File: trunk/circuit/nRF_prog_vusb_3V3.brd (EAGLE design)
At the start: 50 x 50 mm, 26 parts, among them Q2 12MHz

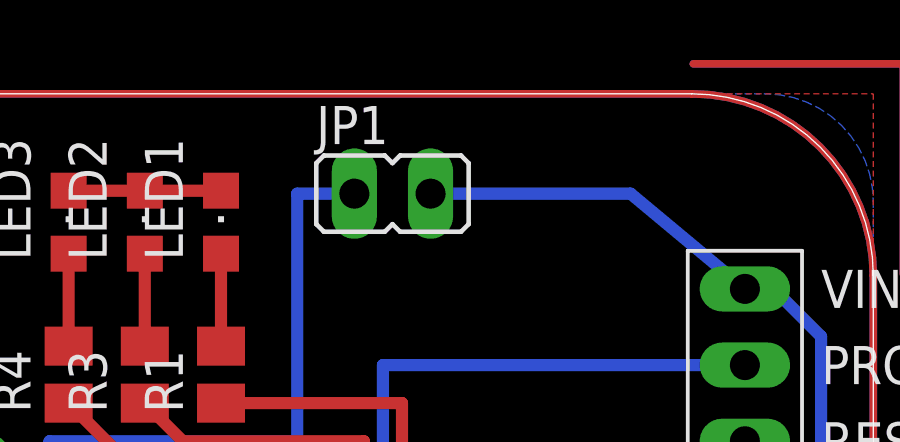
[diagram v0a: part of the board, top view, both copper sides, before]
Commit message: 
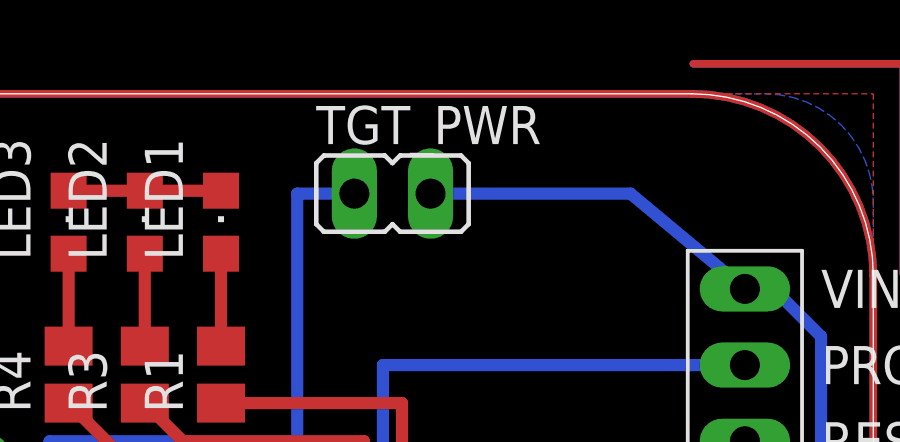
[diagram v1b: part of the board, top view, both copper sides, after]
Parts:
- renumbered JP1 to TGT_PWR
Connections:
- new net NRF_RESET: U$2.RESET
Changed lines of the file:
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@@
 <element name="LED1" library="led" package="CHIPLED_0805" value="" x="28.2575" y="45.72"/>
 <element name="R1" library="rcl" package="M0805" value="" x="28.2575" y="40.64" rot="R90"/>
-<element name="JP1" library="KileParts" package="JP1" value="TGT_PWR" x="33.9725" y="46.6725" rot="R270"/>
+<element name="TGT_PWR" library="KileParts" package="JP1" value="TGT_PWR" x="33.9725" y="46.6725" rot="R270"/>
 <element name="C2" library="rcl" package="C0805K" value="470nF" x="14.605" y="20.6375"/>
 <element name="R2" library="rcl" package="M0805" value="10K" x="18.7325" y="13.97" rot="R270"/>
@@
 <signal name="VIN">
 <contactref element="NRF_GEN" pad="VUSB"/>
-<contactref element="JP1" pad="2"/>
+<contactref element="TGT_PWR" pad="2"/>
 <contactref element="U$2" pad="VIN"/>
 <contactref element="C5" pad="+"/>
@@
 <contactref element="LM3940" pad="1"/>
 <contactref element="C2" pad="1"/>
-<contactref element="JP1" pad="1"/>
+<contactref element="TGT_PWR" pad="1"/>
 <wire x1="9.545" y1="40.2463" x2="9.545" y2="36.83" width="0.4064" layer="16"/>
 <wire x1="30.7975" y1="38.4175" x2="30.7975" y2="46.6725" width="0.4064" layer="16"/>
@@
 <wire x1="51" y1="-1" x2="44" y2="-1" width="0.254" layer="16"/>
 </signal>
+<signal name="NRF_RESET">
+<contactref element="U$2" pad="RESET"/>
+</signal>
 </signals>

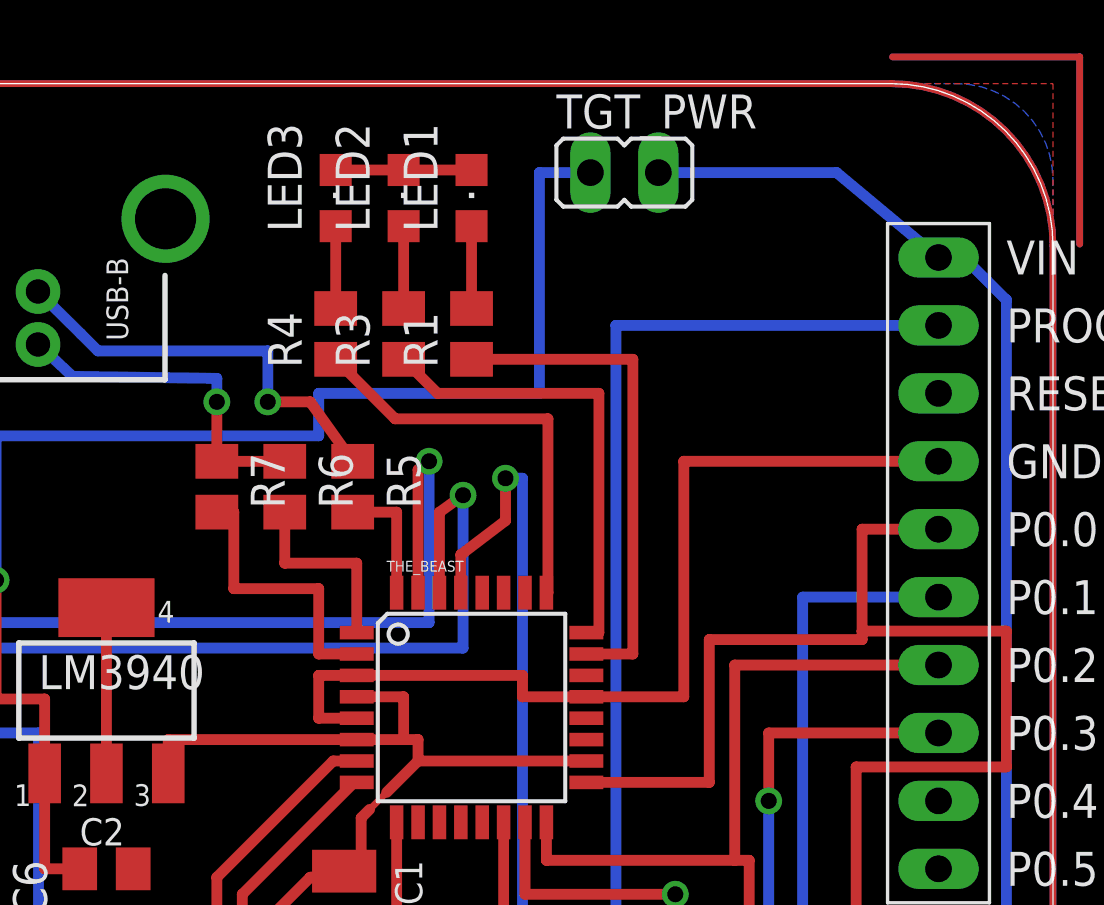
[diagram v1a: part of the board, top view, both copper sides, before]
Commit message: New version works uses reset which hopefully fixes the problems with programming nRF24LU1+ It looks like it is necessary to reset the target before and/or after programming.
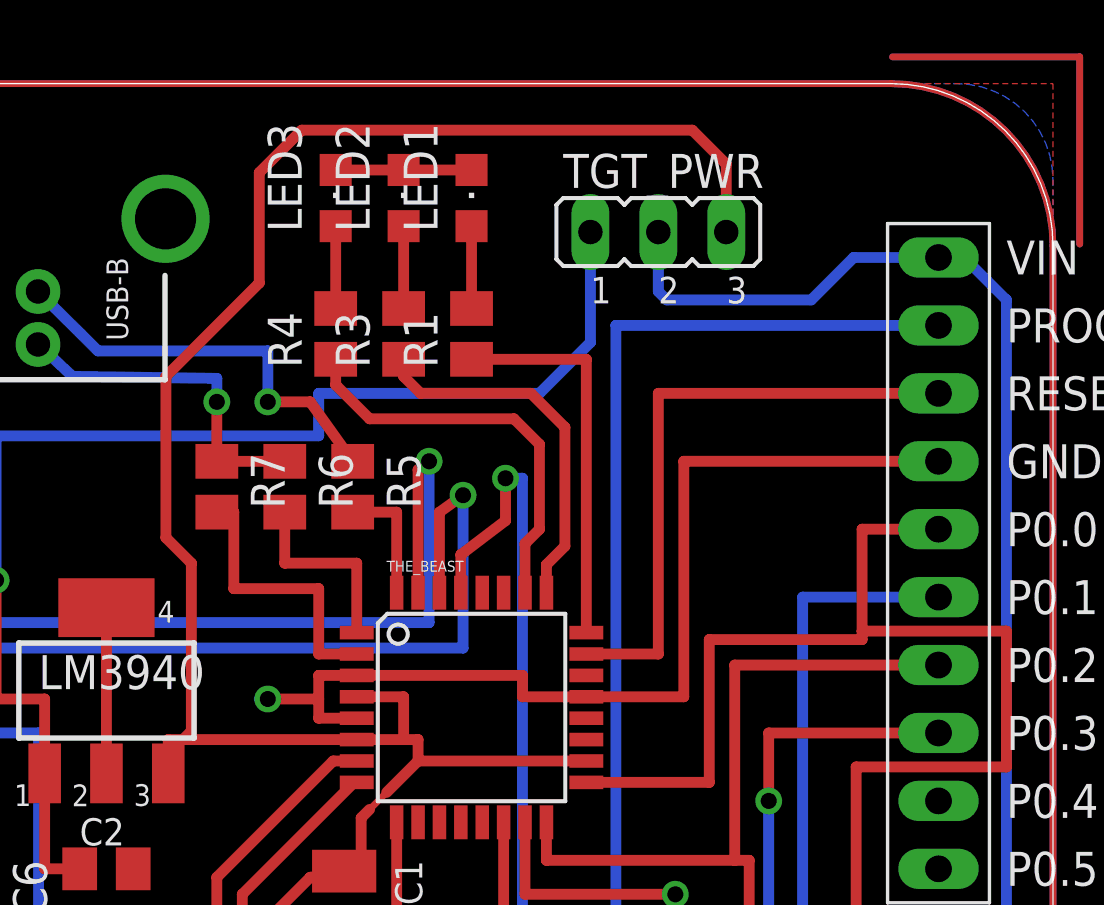
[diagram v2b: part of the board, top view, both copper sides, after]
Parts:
- TGT_PWR: value TGT_PWR -> (none); device KileParts:JP1 -> jumper:JP2
- moved TGT_PWR 2.56 mm to (35.2, 44.5), turned to 0 degrees
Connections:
- removed net N$17: R4.1, THE_BEAST.25
- removed net NRF_RESET: U$2.RESET
- new net N$13: R1.1, THE_BEAST.24
- new net TGT_RST: THE_BEAST.23, U$2.RESET
- net 3.3V: now also TGT_PWR.3
- net N$8: now also R4.1, THE_BEAST.26; no longer R1.1, THE_BEAST.23
- net N$9: now also THE_BEAST.25; no longer THE_BEAST.24
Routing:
- net 3.3V: track 104.8 -> 149.2 mm
- net TGT_RST: track 0.00 -> 22.9 mm
- net N$17: track 15.4 -> 0.00 mm
- net N$13: track 0.00 -> 14.5 mm
- net N$8: track 18.8 -> 15.3 mm
- net VBUS: track 55.7 -> 52.4 mm
- net N$9: track 17.2 -> 13.9 mm
- net GND: track 175.1 -> 177.3 mm, vias 0 -> 1
- net VIN: track 69.7 -> 71.6 mm
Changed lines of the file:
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@@
 <element name="LED1" library="led" package="CHIPLED_0805" value="" x="28.2575" y="45.72"/>
 <element name="R1" library="rcl" package="M0805" value="" x="28.2575" y="40.64" rot="R90"/>
-<element name="TGT_PWR" library="KileParts" package="JP1" value="TGT_PWR" x="33.9725" y="46.6725" rot="R270"/>
 <element name="C2" library="rcl" package="C0805K" value="470nF" x="14.605" y="20.6375"/>
 <element name="R2" library="rcl" package="M0805" value="10K" x="18.7325" y="13.97" rot="R270"/>
@@
 <element name="C6" library="rcl" package="C0805" value="20pF" x="9.8425" y="19.685" rot="R270"/>
 <element name="C3" library="rcl" package="C0805" value="20pF" x="9.8425" y="15.875" rot="R90"/>
+<element name="TGT_PWR" library="jumper" package="JP2" value="" x="35.2425" y="44.45"/>
 </elements>
 <signals>
@@
 <wire x1="10.16" y1="20.635" x2="10.16" y2="23.8125" width="0.4064" layer="1"/>
 <wire x1="23.9649" y1="27.87" x2="22.5425" y2="27.87" width="0.4064" layer="1"/>
-<wire x1="22.5425" y1="27.87" x2="22.5425" y2="26.27" width="0.4064" layer="1"/>
+<wire x1="22.5425" y1="27.87" x2="22.5425" y2="26.9875" width="0.4064" layer="1"/>
 <wire x1="22.5425" y1="26.27" x2="23.9649" y2="26.27" width="0.4064" layer="1"/>
 <wire x1="23.9649" y1="27.87" x2="30.1625" y2="27.87" width="0.4064" layer="1"/>
@@
 </polygon>
 <contactref element="R2" pad="2"/>
+<wire x1="22.5425" y1="26.27" x2="22.5425" y2="26.9875" width="0.4064" layer="1"/>
+<wire x1="22.5425" y1="26.9875" x2="20.6375" y2="26.9875" width="0.4064" layer="1"/>
+<via x="20.6375" y="26.9875" extent="1-16" drill="0.6" shape="square"/>
+<wire x1="20.32" y1="26.9875" x2="20.6375" y2="26.9875" width="0.4064" layer="16"/>
 </signal>
 <signal name="3.3V">
@@
 <wire x1="12.065" y1="25.7175" x2="12.065" y2="13.335" width="0.4064" layer="16"/>
 <wire x1="16.9164" y1="24.2062" x2="16.9164" y2="24.13" width="0.4064" layer="1"/>
-<wire x1="16.9164" y1="25.47" x2="23.9649" y2="25.47" width="0.4064" layer="1"/>
+<wire x1="16.9164" y1="25.47" x2="17.4625" y2="25.47" width="0.4064" layer="1"/>
+<wire x1="17.4625" y1="25.47" x2="23.9649" y2="25.47" width="0.4064" layer="1"/>
 <wire x1="16.9164" y1="25.47" x2="16.9164" y2="24.2062" width="0.4064" layer="1"/>
 <wire x1="18.415" y1="9.8425" x2="18.415" y2="11.1125" width="0.4064" layer="1"/>
@@
 <wire x1="16.51" y1="13.0175" x2="14.2875" y2="13.0175" width="0.4064" layer="1"/>
 <wire x1="14.2875" y1="13.0175" x2="14.2875" y2="13.015" width="0.4064" layer="1"/>
+<contactref element="TGT_PWR" pad="3"/>
+<wire x1="37.7825" y1="44.45" x2="37.7825" y2="46.99" width="0.4064" layer="1"/>
+<wire x1="37.7825" y1="46.99" x2="36.5125" y2="48.26" width="0.4064" layer="1"/>
+<wire x1="36.5125" y1="48.26" x2="21.9075" y2="48.26" width="0.4064" layer="1"/>
+<wire x1="21.9075" y1="48.26" x2="20.32" y2="46.6725" width="0.4064" layer="1"/>
+<wire x1="20.32" y1="46.6725" x2="20.32" y2="42.545" width="0.4064" layer="1"/>
+<wire x1="20.32" y1="42.545" x2="16.8275" y2="39.0525" width="0.4064" layer="1"/>
+<wire x1="16.8275" y1="39.0525" x2="16.8275" y2="33.02" width="0.4064" layer="1"/>
+<wire x1="16.8275" y1="33.02" x2="17.78" y2="32.0675" width="0.4064" layer="1"/>
+<wire x1="17.78" y1="32.0675" x2="17.78" y2="25.7875" width="0.4064" layer="1"/>
+<wire x1="17.78" y1="25.7875" x2="17.4625" y2="25.47" width="0.4064" layer="1"/>
 </signal>
 <signal name="P0.0">
@@
 <signal name="VIN">
 <contactref element="NRF_GEN" pad="VUSB"/>
-<contactref element="TGT_PWR" pad="2"/>
 <contactref element="U$2" pad="VIN"/>
 <contactref element="C5" pad="+"/>
@@
 <wire x1="31.115" y1="2.54" x2="31.115" y2="3.2625" width="0.4064" layer="1"/>
 <wire x1="31.115" y1="3.2625" x2="30.7975" y2="3.2625" width="0.4064" layer="1"/>
-<wire x1="35.2425" y1="46.6725" x2="41.91" y2="46.6725" width="0.4064" layer="16"/>
-<wire x1="41.91" y1="46.6725" x2="45.72" y2="43.4975" width="0.4064" layer="16"/>
 <wire x1="46.64" y1="6.0325" x2="46.64" y2="5.08" width="0.4064" layer="1"/>
 <wire x1="46.64" y1="5.08" x2="44.1" y2="2.54" width="0.4064" layer="1"/>
 <wire x1="45.72" y1="43.4975" x2="46.6725" y2="43.4975" width="0.4064" layer="16"/>
 <wire x1="46.6725" y1="43.4975" x2="48.26" y2="41.91" width="0.4064" layer="16"/>
+<contactref element="TGT_PWR" pad="2"/>
+<wire x1="35.2425" y1="44.45" x2="35.2425" y2="42.2275" width="0.4064" layer="16"/>
+<wire x1="35.2425" y1="42.2275" x2="35.56" y2="41.91" width="0.4064" layer="16"/>
+<wire x1="35.56" y1="41.91" x2="40.9575" y2="41.91" width="0.4064" layer="16"/>
+<wire x1="40.9575" y1="41.91" x2="42.545" y2="43.4975" width="0.4064" layer="16"/>
+<wire x1="42.545" y1="43.4975" x2="45.72" y2="43.4975" width="0.4064" layer="16"/>
 </signal>
 <signal name="N$26">
@@
 <wire x1="22.5425" y1="31.115" x2="22.5425" y2="28.67" width="0.4064" layer="1"/>
 <wire x1="22.5425" y1="28.67" x2="23.9649" y2="28.67" width="0.4064" layer="1"/>
-</signal>
-<signal name="N$8">
-<contactref element="THE_BEAST" pad="23"/>
-<contactref element="R1" pad="1"/>
-<wire x1="28.2575" y1="39.69" x2="34.29" y2="39.69" width="0.4064" layer="1"/>
-<wire x1="34.29" y1="39.69" x2="34.29" y2="28.67" width="0.4064" layer="1"/>
-<wire x1="34.29" y1="28.67" x2="32.5501" y2="28.67" width="0.4064" layer="1"/>
-</signal>
-<signal name="N$9">
-<contactref element="R3" pad="1"/>
-<contactref element="THE_BEAST" pad="24"/>
-<wire x1="25.7175" y1="39.69" x2="26.9875" y2="38.4175" width="0.4064" layer="1"/>
-<wire x1="26.9875" y1="38.4175" x2="33.02" y2="38.4175" width="0.4064" layer="1"/>
-<wire x1="33.02" y1="38.4175" x2="33.02" y2="29.47" width="0.4064" layer="1"/>
-<wire x1="33.02" y1="29.47" x2="32.5501" y2="29.47" width="0.4064" layer="1"/>
-</signal>
-<signal name="N$17">
-<contactref element="THE_BEAST" pad="25"/>
-<contactref element="R4" pad="1"/>
-<wire x1="23.1775" y1="39.69" x2="25.4" y2="37.465" width="0.4064" layer="1"/>
-<wire x1="25.4" y1="37.465" x2="31.115" y2="37.465" width="0.4064" layer="1"/>
-<wire x1="31.115" y1="37.465" x2="31.115" y2="30.9626" width="0.4064" layer="1"/>
-<wire x1="31.115" y1="30.9626" x2="31.0575" y2="30.9626" width="0.4064" layer="1"/>
 </signal>
 <signal name="N$18">
@@
 <contactref element="LM3940" pad="1"/>
 <contactref element="C2" pad="1"/>
-<contactref element="TGT_PWR" pad="1"/>
 <wire x1="9.545" y1="40.2463" x2="9.545" y2="36.83" width="0.4064" layer="16"/>
-<wire x1="30.7975" y1="38.4175" x2="30.7975" y2="46.6725" width="0.4064" layer="16"/>
-<wire x1="30.7975" y1="46.6725" x2="32.7025" y2="46.6725" width="0.4064" layer="16"/>
 <wire x1="30.7975" y1="38.4175" x2="22.5425" y2="38.4175" width="0.4064" layer="16"/>
 <wire x1="22.5425" y1="38.4175" x2="22.5425" y2="36.83" width="0.4064" layer="16"/>
@@
 <wire x1="12.2936" y1="26.9875" x2="10.4775" y2="26.9875" width="0.4064" layer="1"/>
 <wire x1="10.4775" y1="26.9875" x2="10.4775" y2="31.4325" width="0.4064" layer="1"/>
+<contactref element="TGT_PWR" pad="1"/>
+<wire x1="32.7025" y1="44.45" x2="32.7025" y2="40.3225" width="0.4064" layer="16"/>
+<wire x1="32.7025" y1="40.3225" x2="30.7975" y2="38.4175" width="0.4064" layer="16"/>
 </signal>
 <signal name="N$1">
@@
 <wire x1="51" y1="-1" x2="44" y2="-1" width="0.254" layer="16"/>
 </signal>
-<signal name="NRF_RESET">
+<signal name="TGT_RST">
 <contactref element="U$2" pad="RESET"/>
+<contactref element="THE_BEAST" pad="23"/>
+<wire x1="45.72" y1="38.4175" x2="35.2425" y2="38.4175" width="0.4064" layer="1"/>
+<wire x1="35.2425" y1="38.4175" x2="35.2425" y2="28.67" width="0.4064" layer="1"/>
+<wire x1="35.2425" y1="28.67" x2="32.5501" y2="28.67" width="0.4064" layer="1"/>
+</signal>
+<signal name="N$8">
+<contactref element="R4" pad="1"/>
+<contactref element="THE_BEAST" pad="26"/>
+<wire x1="30.2575" y1="30.9626" x2="30.2575" y2="32.7975" width="0.4064" layer="1"/>
+<wire x1="30.2575" y1="32.7975" x2="30.7975" y2="33.3375" width="0.4064" layer="1"/>
+<wire x1="30.7975" y1="33.3375" x2="30.7975" y2="36.5125" width="0.4064" layer="1"/>
+<wire x1="30.7975" y1="36.5125" x2="29.845" y2="37.465" width="0.4064" layer="1"/>
+<wire x1="29.845" y1="37.465" x2="24.4475" y2="37.465" width="0.4064" layer="1"/>
+<wire x1="23.1775" y1="39.69" x2="23.1775" y2="38.735" width="0.4064" layer="1"/>
+<wire x1="23.1775" y1="38.735" x2="24.4475" y2="37.465" width="0.4064" layer="1"/>
+</signal>
+<signal name="N$9">
+<contactref element="R3" pad="1"/>
+<contactref element="THE_BEAST" pad="25"/>
+<wire x1="25.7175" y1="39.69" x2="25.7175" y2="39.0525" width="0.4064" layer="1"/>
+<wire x1="25.7175" y1="39.0525" x2="26.3525" y2="38.4175" width="0.4064" layer="1"/>
+<wire x1="26.3525" y1="38.4175" x2="30.48" y2="38.4175" width="0.4064" layer="1"/>
+<wire x1="30.48" y1="38.4175" x2="31.75" y2="37.1475" width="0.4064" layer="1"/>
+<wire x1="31.75" y1="37.1475" x2="31.75" y2="32.7025" width="0.4064" layer="1"/>
+<wire x1="31.75" y1="32.7025" x2="31.0575" y2="32.01" width="0.4064" layer="1"/>
+<wire x1="31.0575" y1="32.01" x2="31.0575" y2="30.9626" width="0.4064" layer="1"/>
+</signal>
+<signal name="N$13">
+<contactref element="R1" pad="1"/>
+<contactref element="THE_BEAST" pad="24"/>
+<wire x1="28.2575" y1="39.69" x2="32.5501" y2="39.69" width="0.4064" layer="1"/>
+<wire x1="32.5501" y1="39.69" x2="32.5501" y2="29.47" width="0.4064" layer="1"/>
 </signal>
 </signals>

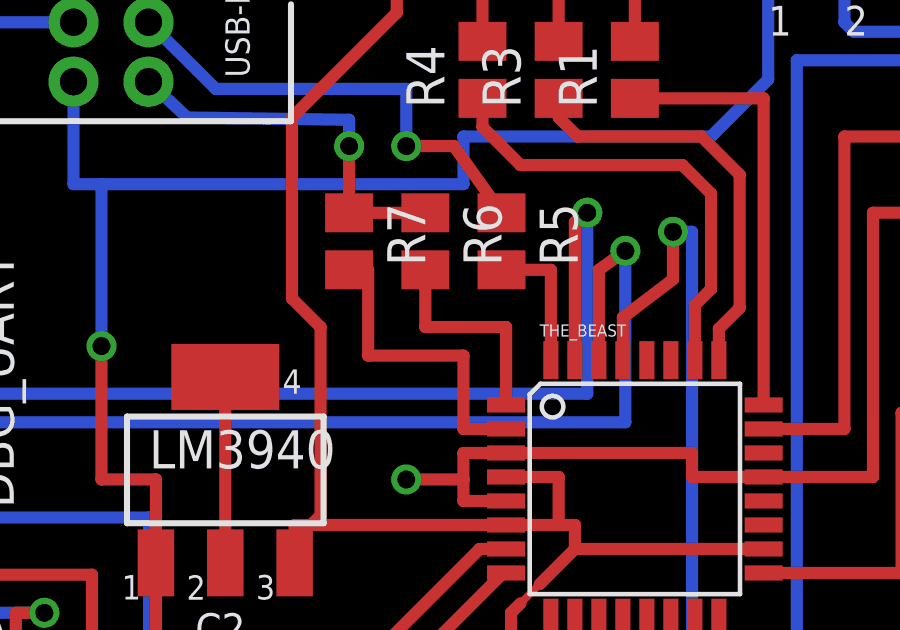
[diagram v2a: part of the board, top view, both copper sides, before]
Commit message: 
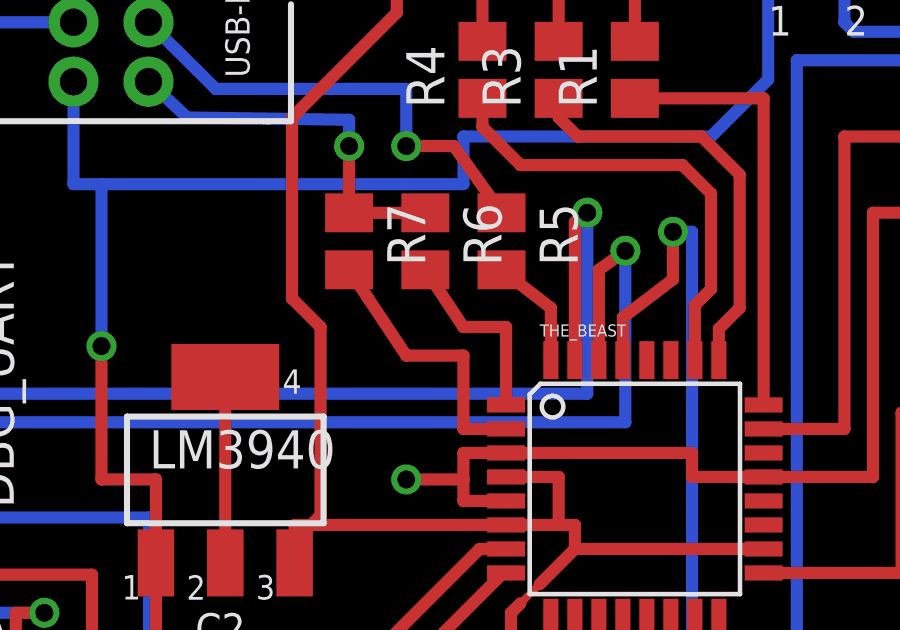
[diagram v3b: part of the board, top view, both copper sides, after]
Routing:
- net DPULLUP: track 10.5 -> 9.21 mm
- net D-: track 7.20 -> 6.31 mm
- net D+: track 4.66 -> 3.82 mm
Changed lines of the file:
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@@
 <contactref element="THE_BEAST" pad="32"/>
 <contactref element="R5" pad="2"/>
-<wire x1="23.8125" y1="33.975" x2="25.4575" y2="33.975" width="0.4064" layer="1"/>
-<wire x1="25.4575" y1="33.975" x2="25.4575" y2="30.9626" width="0.4064" layer="1"/>
+<wire x1="23.8125" y1="33.975" x2="25.4575" y2="32.705" width="0.4064" layer="1"/>
+<wire x1="25.4575" y1="32.705" x2="25.4575" y2="30.9626" width="0.4064" layer="1"/>
 </signal>
 <signal name="D-">
 <contactref element="THE_BEAST" pad="1"/>
 <contactref element="R6" pad="2"/>
-<wire x1="21.2725" y1="33.975" x2="21.2725" y2="32.0675" width="0.4064" layer="1"/>
-<wire x1="21.2725" y1="32.0675" x2="23.9649" y2="32.0675" width="0.4064" layer="1"/>
+<wire x1="21.2725" y1="33.975" x2="22.5425" y2="32.0675" width="0.4064" layer="1"/>
+<wire x1="22.5425" y1="32.0675" x2="23.9649" y2="32.0675" width="0.4064" layer="1"/>
 <wire x1="23.9649" y1="32.0675" x2="23.9649" y2="29.47" width="0.4064" layer="1"/>
 </signal>
@@
 <contactref element="THE_BEAST" pad="2"/>
 <contactref element="R7" pad="2"/>
-<wire x1="18.7325" y1="33.975" x2="19.3675" y2="33.975" width="0.4064" layer="1"/>
-<wire x1="19.3675" y1="33.975" x2="19.3675" y2="31.115" width="0.4064" layer="1"/>
-<wire x1="19.3675" y1="31.115" x2="22.5425" y2="31.115" width="0.4064" layer="1"/>
+<wire x1="18.7325" y1="33.975" x2="19.3675" y2="33.0225" width="0.4064" layer="1"/>
+<wire x1="19.3675" y1="33.0225" x2="20.6375" y2="31.115" width="0.4064" layer="1"/>
+<wire x1="20.6375" y1="31.115" x2="22.5425" y2="31.115" width="0.4064" layer="1"/>
 <wire x1="22.5425" y1="31.115" x2="22.5425" y2="28.67" width="0.4064" layer="1"/>
 <wire x1="22.5425" y1="28.67" x2="23.9649" y2="28.67" width="0.4064" layer="1"/>
